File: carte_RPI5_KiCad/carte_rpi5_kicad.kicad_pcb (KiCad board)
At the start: 2 copper layers, 25 parts, among them J0 Vin batterie, J1 Conn_01x03, J2 Conn_01x03, J3 Conn_01x03, J4 Conn_01x03, J5 Conn_01x03, J6 Conn_01x03, J7 Conn_01x03, J8 Conn_01x03, SW1 SW_SPDT

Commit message: mise à jour PCB
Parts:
- removed J0: Vin batterie, Connector_AMASS:AMASS_XT60-F_1x02_P7.20mm_Vertical
- removed R_Pull_Up1: 1 k, Resistor_SMD:R_0805_2012Metric
- removed R_SCL1, R_SDA1: 4,7k, Resistor_SMD:R_0805_2012Metric
- removed Raspberry5: CM5108032, Connector_PinSocket_2.54mm:PinSocket_2x20_P2.54mm_Vertical
- added J10: RPI5_40pins, Connector_PinSocket_2.54mm:PinSocket_2x20_P2.54mm_Vertical, F.Cu at (143.6, 109.0)
- added J9: XT60-M, Connector_AMASS:AMASS_XT60-F_1x02_P7.20mm_Vertical, F.Cu at (189.1, 89.5)
- added R_SCL2: 4,7k, Resistor_SMD:R_0805_2012Metric, F.Cu at (134.8, 70.8)
- added R_SDA2: 4,7k, Resistor_SMD:R_0805_2012Metric, F.Cu at (104.3, 96.1)
- SW1: footprint Button_Switch_THT:SW_DIP_SPSTx01_Slide_6.7x4.1mm_W7.62mm_P2.54mm_LowProfile -> Button_Switch_THT:SW_Slide_SPDT_Straight_CK_OS102011MS2Q
- moved F1 73.1 mm to (183.5, 74.9)
- moved SW1 67.7 mm to (170.6, 67.5), turned to -90 degrees
- moved Conn_luna1 53.0 mm to (82.8, 91.6)
- moved Conn_BNO1 51.2 mm to (75.5, 91.5)
- moved D1 50.2 mm to (159.3, 85.7), turned to 90 degrees
- moved Pont_en_H1 44.7 mm to (152.9, 95.4), turned to 180 degrees
- moved Régulateur_de_tension1 43.6 mm to (175.1, 84.5)
- moved R2 38.2 mm to (178.4, 94.7), turned to 180 degrees
- moved Conn_Treuil_Pince1 28.8 mm to (145.3, 73.0), turned to 90 degrees
- moved Conn_LPS22HB1 24.7 mm to (89.6, 84.7)
- moved R1 23.0 mm to (164.1, 85.8), turned to -90 degrees
- moved J5 17.8 mm to (120.4, 78.0)
- moved J6 17.8 mm to (125.0, 78.0)
- moved J1 17.8 mm to (102.0, 78.0)
- moved J2 17.8 mm to (106.6, 78.0)
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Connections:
- SW1 pad 1: Net-(Régulateur_de_tension1-ON/OFF_CONTROL) -> Net-(Régulateur_de_tension1-VIN)
- SW1 pad 2: GND -> Net-(Régulateur_de_tension1-ON/OFF_CONTROL)
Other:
- board outline added: 135 x 58.9 mm

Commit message: Mise à jour du PCB
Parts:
- added ?: , clipboard:6f5e2fe0-dd56-4c47-aeb5-3915356e93c1, F.Cu at (178.7, 114.0)
- F1: footprint Fuse:Fuse_0402_1005Metric -> librairie_empreintes:PTF-50
- moved J4 26.1 mm to (89.8, 75.5)
- moved J1 26.1 mm to (76.0, 75.5)
- moved J2 26.1 mm to (80.6, 75.5)
- moved J3 26.1 mm to (85.2, 75.5)
- moved R_SDA2 24.9 mm to (80.9, 104.5)
- moved J9 18.9 mm to (176.4, 103.5)
- moved Régulateur_de_tension1 18.0 mm to (163.8, 98.5)
- moved R2 18.0 mm to (166.0, 107.8)
- moved Contrôleur_PWM1 16.8 mm to (130.9, 92.7)
- moved F1 16.0 mm to (168.1, 79.2), turned to 180 degrees
- moved R1 15.0 mm to (154.5, 97.3)
- moved D1 14.1 mm to (151.2, 97.2)
- moved R_SCL2 10.8 mm to (134.2, 81.6)
- moved J7 6.94 mm to (131.8, 71.4)
- moved J8 6.94 mm to (136.4, 71.4)
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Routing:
- added copper zone on B.Cu, net GND
- added copper zone on F.Cu, net GND
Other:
- board size 135 x 58.9 mm -> 121 x 58.9 mm

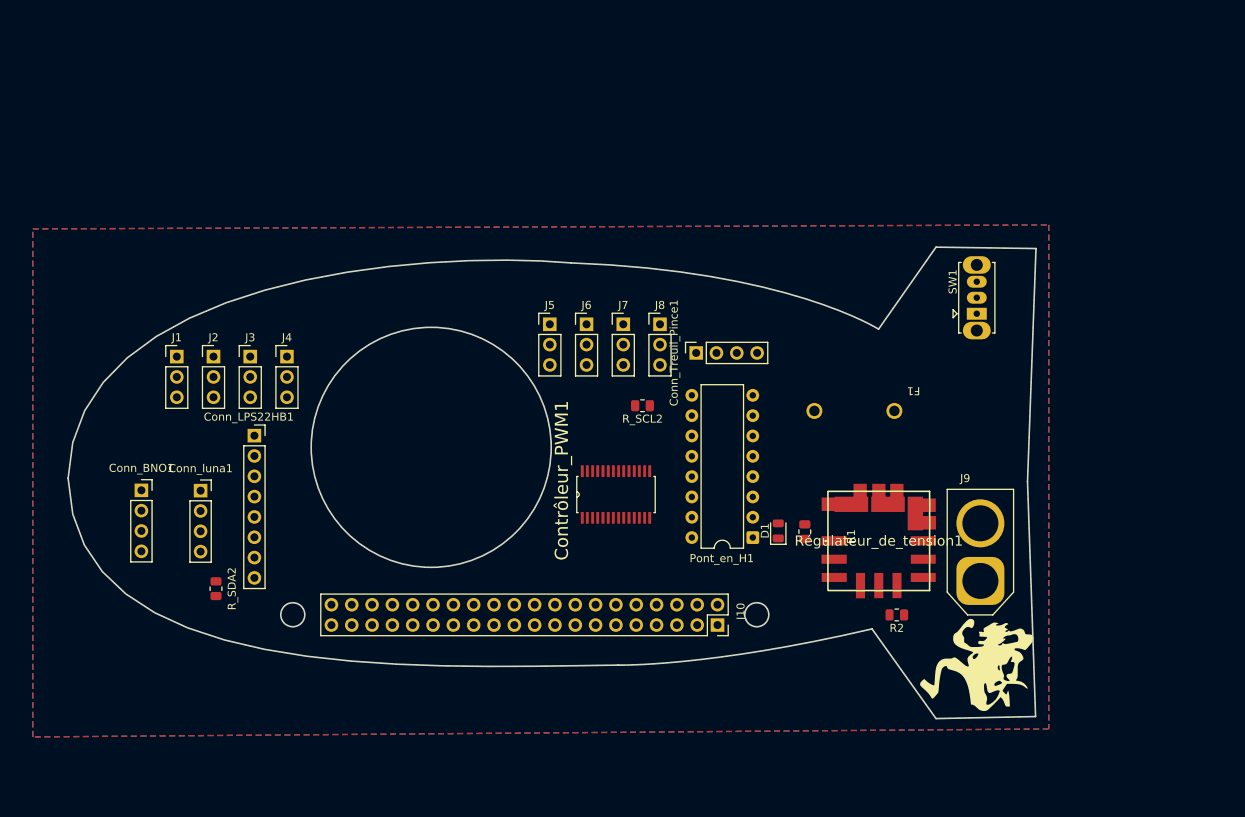
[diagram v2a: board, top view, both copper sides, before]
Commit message: Deuxième version du routage pour le PCB
Il y a encore pas mal d'erreurs au niveau des pads, voir la taille minimale acceptable des pistes pour chaque composant.
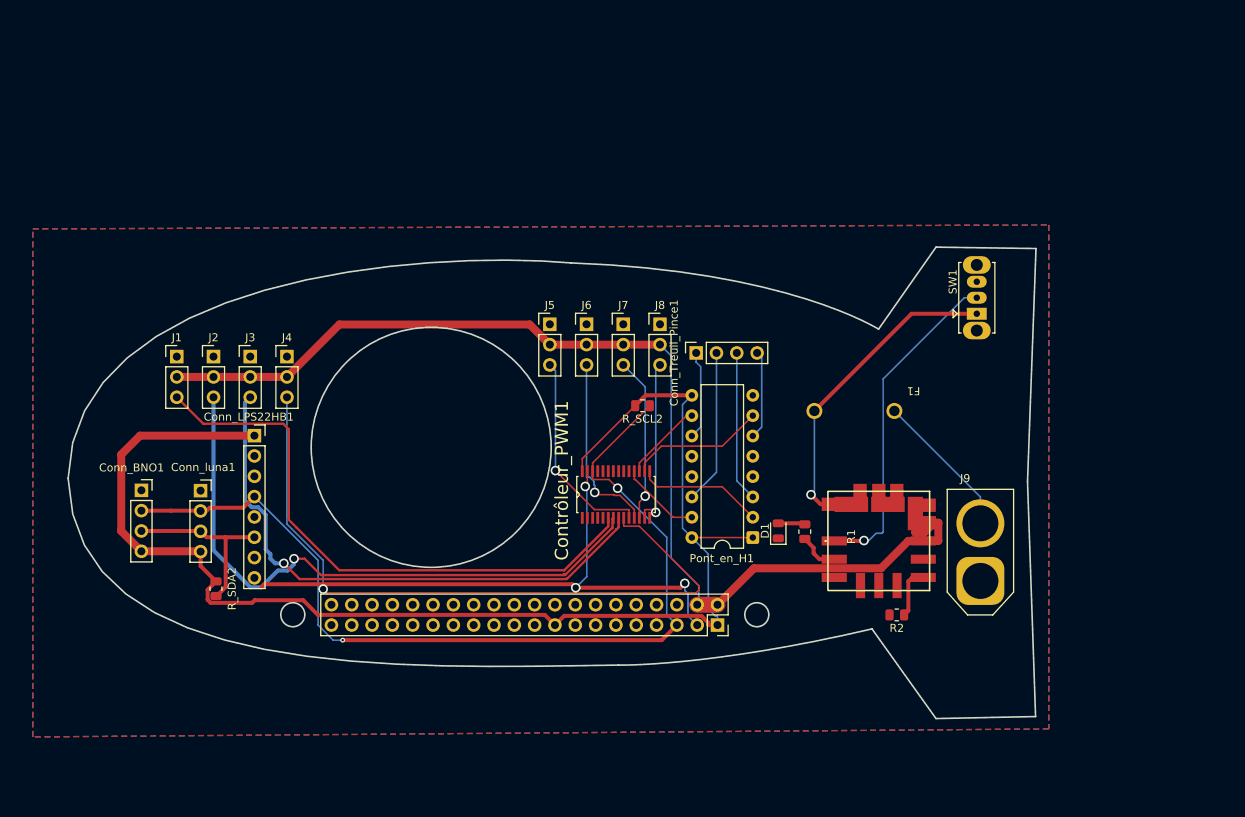
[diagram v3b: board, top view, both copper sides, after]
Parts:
- removed ?: , clipboard:6f5e2fe0-dd56-4c47-aeb5-3915356e93c1
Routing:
- net 3.3V: track 0.00 -> 169.2 mm
- net 5V: track 0.00 -> 144.7 mm
- net SCL: track 0.00 -> 120.3 mm, vias 0 -> 2
- net SDA: track 0.00 -> 97.0 mm, vias 0 -> 3
- net PWM3: track 0.00 -> 87.2 mm, vias 0 -> 1
- net PWM1: track 0.00 -> 77.6 mm, vias 0 -> 1
- net PWM0: track 0.00 -> 72.9 mm
- net PWM2: track 0.00 -> 70.7 mm, vias 0 -> 1
- net Net-(Régulateur_de_tension1-VIN): track 0.00 -> 43.0 mm, vias 0 -> 1
- net Net-(Régulateur_de_tension1-ON/OFF_CONTROL): track 0.00 -> 41.8 mm, vias 0 -> 1
- net PWM4: track 0.00 -> 25.8 mm, vias 0 -> 1
- net PWM5: track 0.00 -> 23.5 mm, vias 0 -> 1
- net PWM7: track 0.00 -> 21.2 mm, vias 0 -> 1
- net PWM6: track 0.00 -> 20.6 mm, vias 0 -> 1
- net Mot_pince-: track 0.00 -> 19.3 mm
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
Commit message: Agrandissement + recablage du PCB
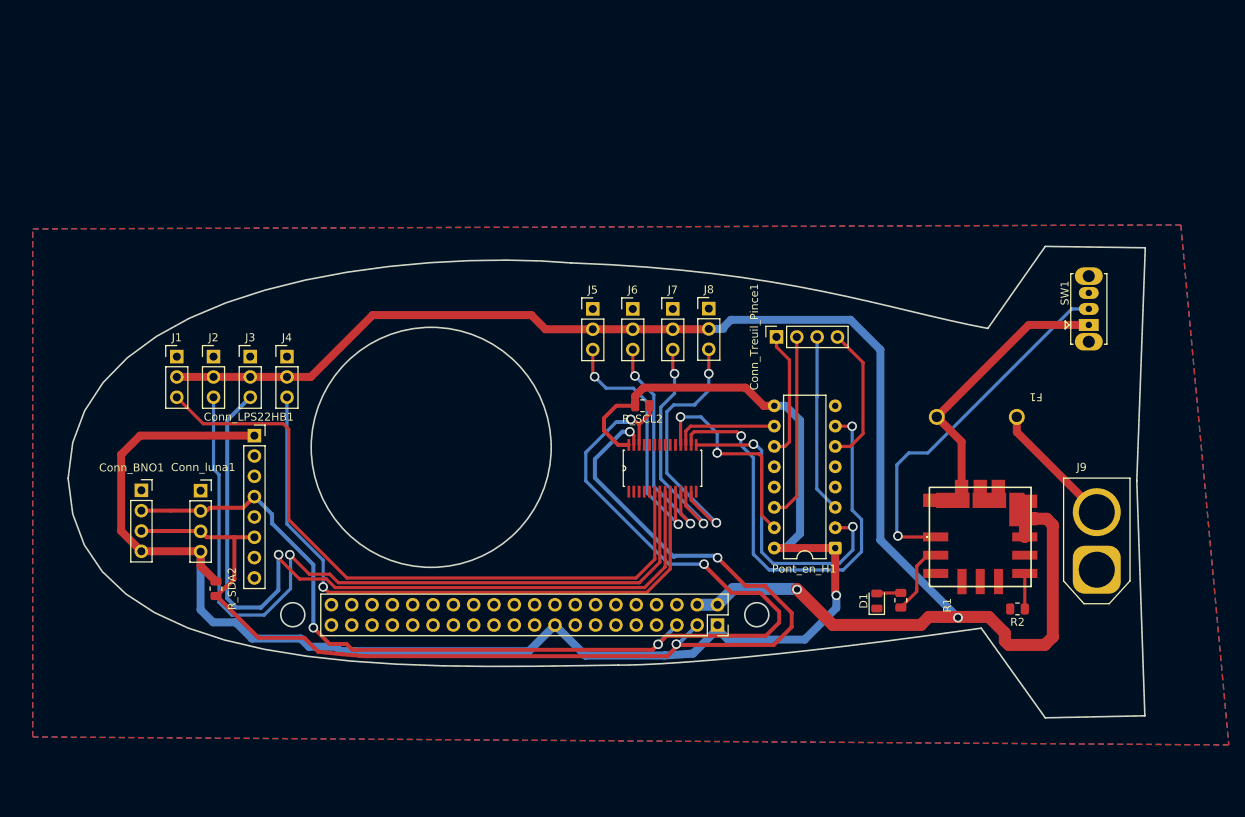
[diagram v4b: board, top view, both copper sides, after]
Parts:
- moved F1 15.3 mm to (183.4, 80.0)
- moved D1 15.1 mm to (163.5, 106.0)
- moved R2 15.1 mm to (181.1, 107.0)
- moved R1 14.7 mm to (166.5, 105.9)
- moved J9 14.6 mm to (191.0, 102.1)
- moved SW1 14.1 mm to (190.0, 71.5)
- moved Régulateur_de_tension1 12.7 mm to (176.4, 98.0)
- moved Pont_en_H1 10.4 mm to (158.3, 99.4)
- moved Conn_Treuil_Pince1 10.2 mm to (151.0, 73.0)
- moved Contrôleur_PWM1 6.67 mm to (136.7, 89.4)
- moved J7 6.48 mm to (138.0, 69.5)
- moved J8 6.41 mm to (142.5, 69.5)
- moved J6 6.09 mm to (133.0, 69.5)
- moved J5 5.70 mm to (128.0, 69.5)
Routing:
- net 5V: track 144.7 -> 204.1 mm, vias 0 -> 2
- net SDA: track 97.0 -> 146.6 mm
- net PWM9: track 17.0 -> 56.8 mm, vias 0 -> 2
- net 3.3V: track 169.2 -> 206.3 mm, vias 0 -> 1
- net SCL: track 120.3 -> 154.3 mm, vias 2 -> 4
- net PWM2: track 70.7 -> 99.5 mm
- net PWM8: track 15.9 -> 38.9 mm, vias 0 -> 2
- net PWM1: track 77.6 -> 98.8 mm
- net PWM11: track 10.2 -> 26.7 mm, vias 0 -> 2
- net PWM0: track 72.9 -> 85.1 mm
- net PWM7: track 21.2 -> 33.4 mm, vias 1 -> 2
- net PWM6: track 20.6 -> 29.7 mm, vias 1 -> 2
- net Net-(Régulateur_de_tension1-VIN): track 43.0 -> 34.5 mm, vias 1 -> 0
- net PWM3: track 87.2 -> 80.4 mm
- net PWM4: track 25.8 -> 32.5 mm, vias 1 -> 2
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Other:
- board size 121 x 58.9 mm -> 134.6 x 58.9 mm

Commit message: Mise à jour PCB
Correction des erreurs sur les pistes / via, ajouts de sérigraphie, logos et vérification du PCB, il reste malgré tout une erreur indiquant que les deux plans de masses de sont pas reliés même avec l'ajout d'un via pour cela.
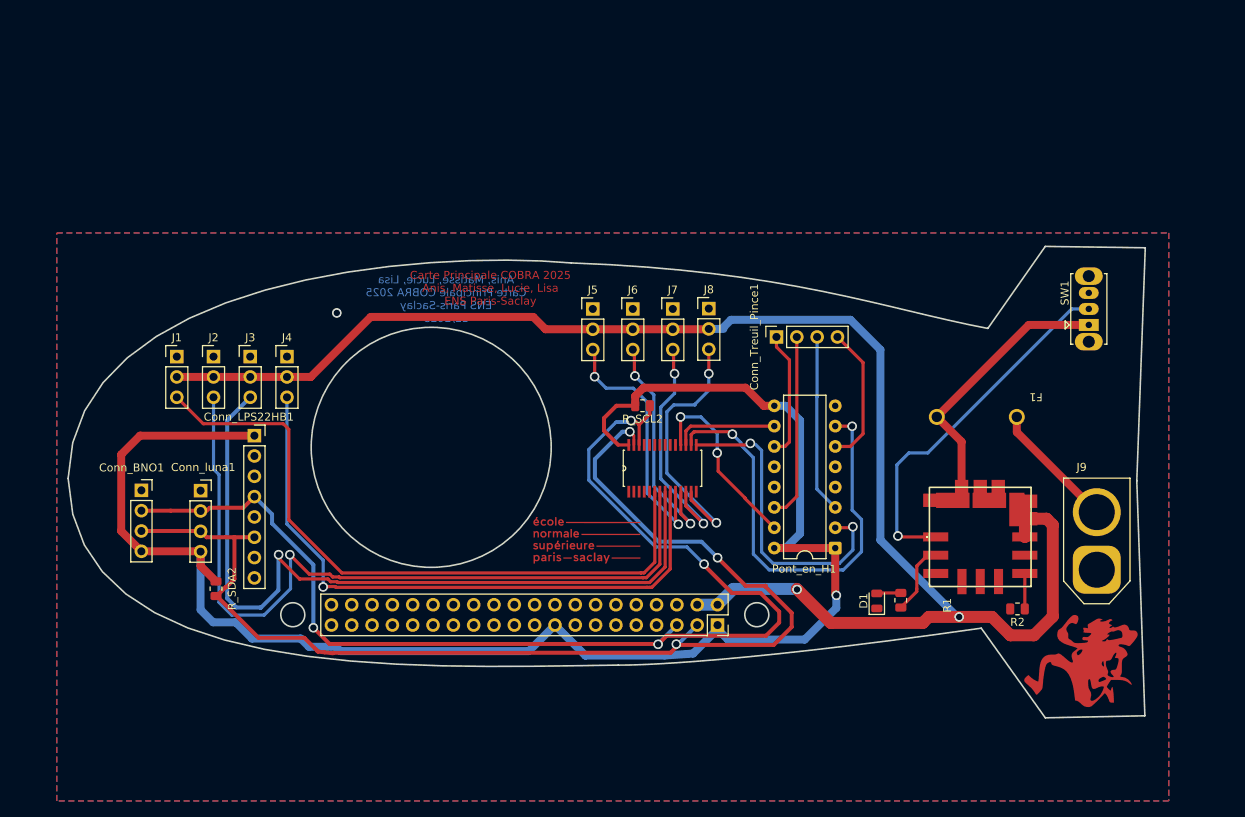
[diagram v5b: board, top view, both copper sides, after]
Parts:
- added ?: , clipboard:6f5e2fe0-dd56-4c47-aeb5-3915356e93c1, F.Cu at (191.8, 113.5)
- added G***: LOGO, LOGO, F.Cu at (127.2, 98.4)
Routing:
- net 5V: track 204.1 -> 200.7 mm
- net PWM11: track 26.7 -> 23.7 mm
- net SCL: track 154.3 -> 153.1 mm
- net PWM2: track 99.5 -> 98.9 mm
- net GND: vias 0 -> 1
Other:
- board text added: "Anis, Matisse, Lucie, Lisa Carte Principale COBRA 2025 ENS Paris-Saclay 12/2025"
- board text added: "Carte Principale COBRA 2025 Anis, Matisse, Lucie, Lisa ENS Paris-Saclay"

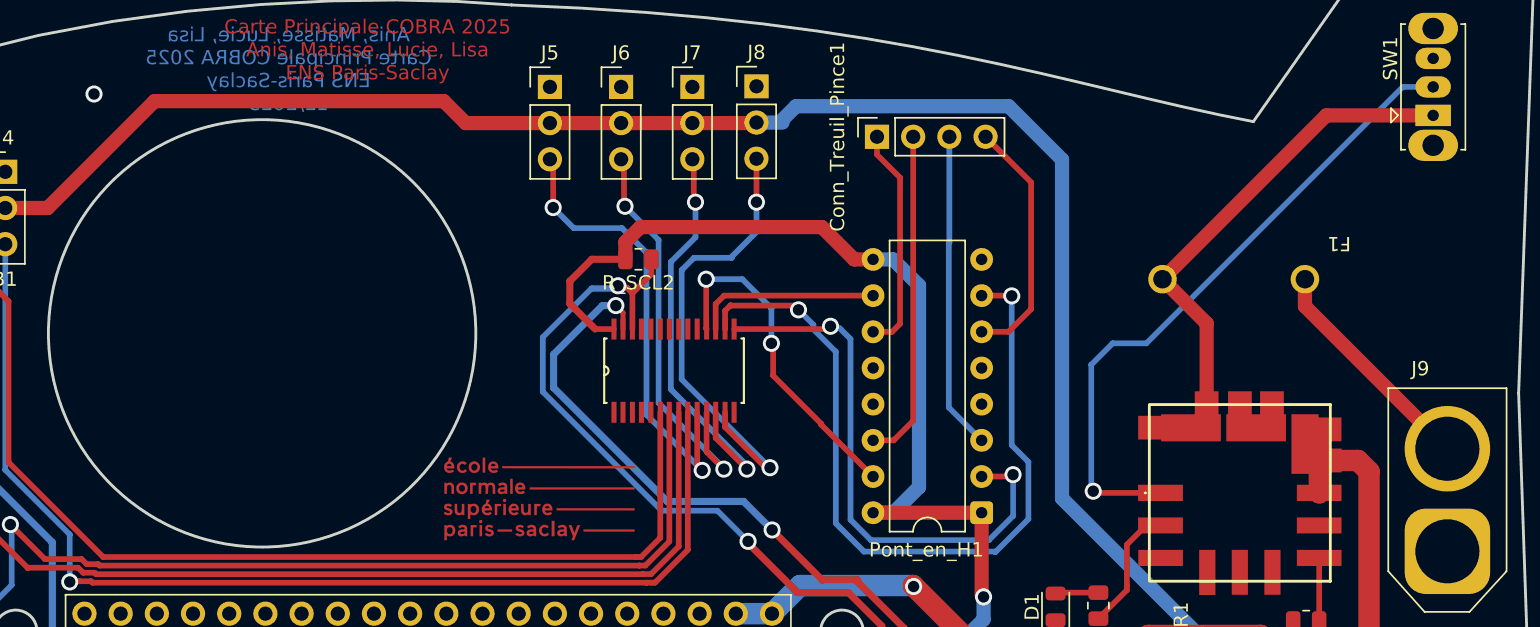
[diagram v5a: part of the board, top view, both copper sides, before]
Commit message: Finalisation du PCB
Toutes les erreurs DRC ont été corrigés. Le PCB est prêt à être tiré.
Anis.
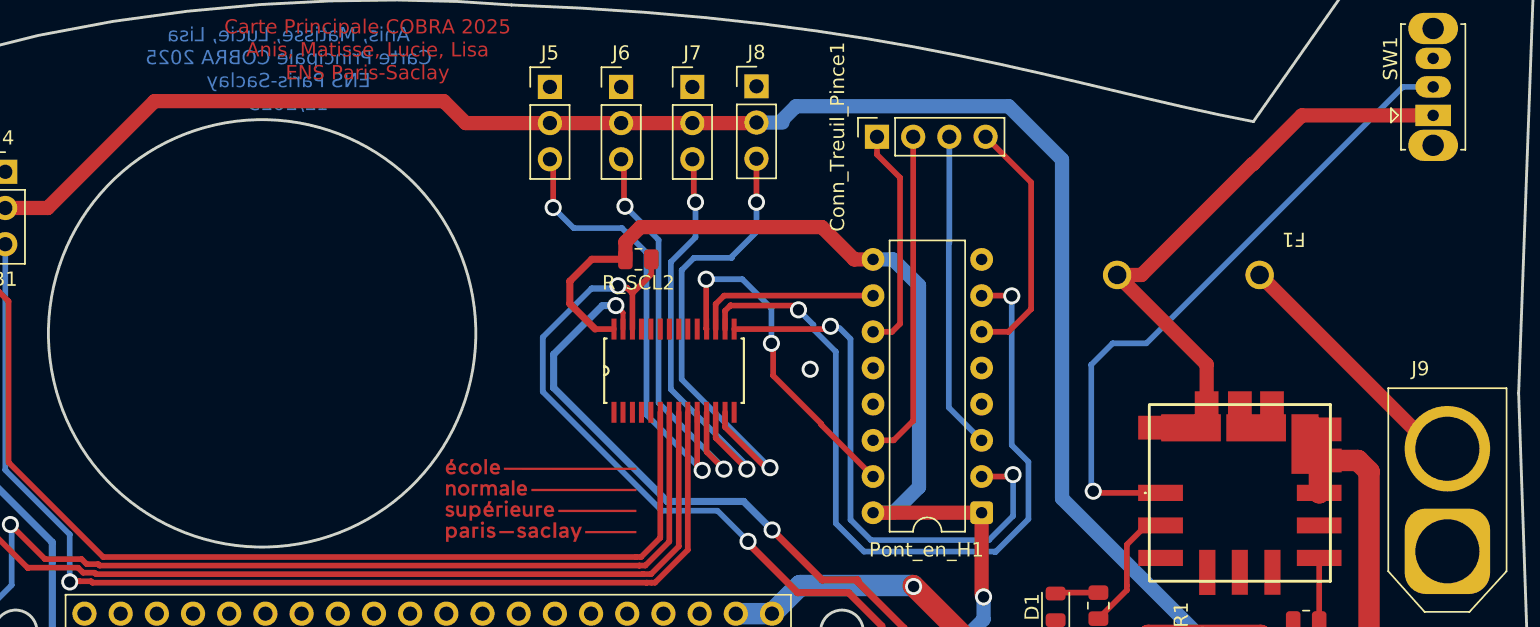
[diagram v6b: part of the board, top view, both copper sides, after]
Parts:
- moved F1 3.19 mm to (180.2, 79.7)
- moved G*** 0.16 mm to (127.3, 98.5)
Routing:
- net Net-(Régulateur_de_tension1-VIN): track 34.5 -> 39.2 mm
- net Net-(J9-POS): track 16.0 -> 18.2 mm
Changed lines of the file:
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@@
 	(footprint "LOGO"
 		(layer "F.Cu")
-		(at 127.21 98.42)
+		(at 127.33 98.53)
 		(property "Reference" "G***"
 			(at 0 0 0)
@@
 	(footprint "librairie_empreintes:PTF-50"
 		(layer "F.Cu")
-		(at 183.4 80 180)
+		(at 180.22 79.7 180)
 		(property "Reference" "F1"
 			(at 0 -0.5 180)
@@
 	)
 	(segment
-		(start 136.24 98.6)
-		(end 128.26 90.62)
+		(start 128.26 90.62)
+		(end 128.26 88.28)
 		(width 0.5)
 		(layer "B.Cu")
@@
 	)
 	(segment
-		(start 128.26 88.28)
-		(end 131.69 84.85)
+		(start 136.24 98.6)
+		(end 128.26 90.62)
 		(width 0.5)
 		(layer "B.Cu")
@@
 	)
 	(segment
-		(start 141.6 98.6)
-		(end 136.24 98.6)
+		(start 131.69 84.85)
+		(end 132.51 84.85)
 		(width 0.5)
 		(layer "B.Cu")
@@
 	)
 	(segment
-		(start 131.69 84.85)
-		(end 132.51 84.85)
+		(start 128.26 88.28)
+		(end 131.69 84.85)
 		(width 0.5)
 		(layer "B.Cu")
@@
 	)
 	(segment
-		(start 128.26 90.62)
-		(end 128.26 88.28)
+		(start 141.6 98.6)
+		(end 136.24 98.6)
 		(width 0.5)
 		(layer "B.Cu")
@@
 	)
 	(segment
-		(start 132.51 84.85)
-		(end 132.57 84.79)
+		(start 143.6 100.6)
+		(end 141.6 98.6)
 		(width 0.5)
 		(layer "B.Cu")
@@
 	)
 	(segment
-		(start 143.6 100.6)
-		(end 141.6 98.6)
+		(start 132.51 84.85)
+		(end 132.57 84.79)
 		(width 0.5)
 		(layer "B.Cu")
@@
 	)
 	(via
-		(at 96 70)
+		(at 146.27 89.32)
 		(size 1.2)
 		(drill 0.8)
@@
 	)
 	(segment
+		(start 180.78 71.5)
+		(end 190 71.5)
+		(width 1)
+		(layer "F.Cu")
+		(net 31)
+	)
+	(segment
+		(start 177.36 74.92)
+		(end 180.78 71.5)
+		(width 1)
+		(layer "F.Cu")
+		(net 31)
+	)
+	(segment
+		(start 169.53 82.7)
+		(end 177.31 74.92)
+		(width 1)
+		(layer "F.Cu")
+		(net 31)
+	)
+	(segment
 		(start 174.099698 92.432003)
-		(end 174.099698 86.099698)
+		(end 174.099698 88.979698)
 		(width 1)
 		(layer "F.Cu")
@@
 	)
 	(segment
-		(start 174.099698 86.099698)
-		(end 171 83)
+		(start 167.82 82.7)
+		(end 169.53 82.7)
 		(width 1)
 		(layer "F.Cu")
@@
 	)
 	(segment
-		(start 182.5 71.5)
-		(end 190 71.5)
+		(start 177.31 74.92)
+		(end 177.36 74.92)
 		(width 1)
 		(layer "F.Cu")
@@
 	)
 	(segment
-		(start 171 83)
-		(end 182.5 71.5)
+		(start 174.099698 88.979698)
+		(end 167.82 82.7)
 		(width 1)
 		(layer "F.Cu")
@@
 	)
 	(segment
-		(start 181 84.9)
-		(end 181 83)
+		(start 191 94.9)
+		(end 190.02 94.9)
 		(width 1)
 		(layer "F.Cu")
@@
 	)
 	(segment
-		(start 191 94.9)
-		(end 181 84.9)
+		(start 190.02 94.9)
+		(end 177.82 82.7)
 		(width 1)
 		(layer "F.Cu")

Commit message: Carte modification version finale
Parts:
- moved J3 4.69 mm to (80.5, 75.5)
- moved J2 4.47 mm to (85.1, 75.5)
- moved R_SDA2 4.38 mm to (76.5, 104.9)
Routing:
- net PWM1: track 98.4 -> 90.9 mm
- net PWM11: track 23.7 -> 16.7 mm, vias 2 -> 0
- net PWM2: track 98.9 -> 92.5 mm
- net 3.3V: track 206.3 -> 211.8 mm, vias 1 -> 2
- net SDA: track 146.3 -> 150.8 mm, vias 3 -> 4
- net SCL: track 153.1 -> 151.2 mm
- net PWM0: track 84.8 -> 86.5 mm, vias 0 -> 1
- net Mot_treuil-: track 17.6 -> 16.0 mm
- net Mot_treuil+: track 22.3 -> 23.9 mm
- net PWM3: track 79.9 -> 81.5 mm
- net Net-(Régulateur_de_tension1-VIN): track 39.2 -> 40.5 mm, vias 0 -> 1
- net Net-(Régulateur_de_tension1-ON/OFF_CONTROL): track 45.7 -> 44.7 mm
- net Net-(J9-POS): track 18.2 -> 19.2 mm
- net Mot_pince-: track 23.3 -> 24.1 mm
- net PWM8: track 38.5 -> 37.9 mm, vias 2 -> 1
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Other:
- board text removed: "Anis, Matisse, Lucie, Lisa Carte Principale COBRA 2025 ENS Paris-Saclay 12/2025"
